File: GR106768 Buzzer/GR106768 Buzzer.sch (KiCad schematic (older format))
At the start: 65 parts, among them IC1 LMC7211, IC2 MC33172, IC3 MC33172, IC4 LMV321, J1 Conn_01x07, T1 BC847, T2 BC857, T3 BC847, T4 BC857

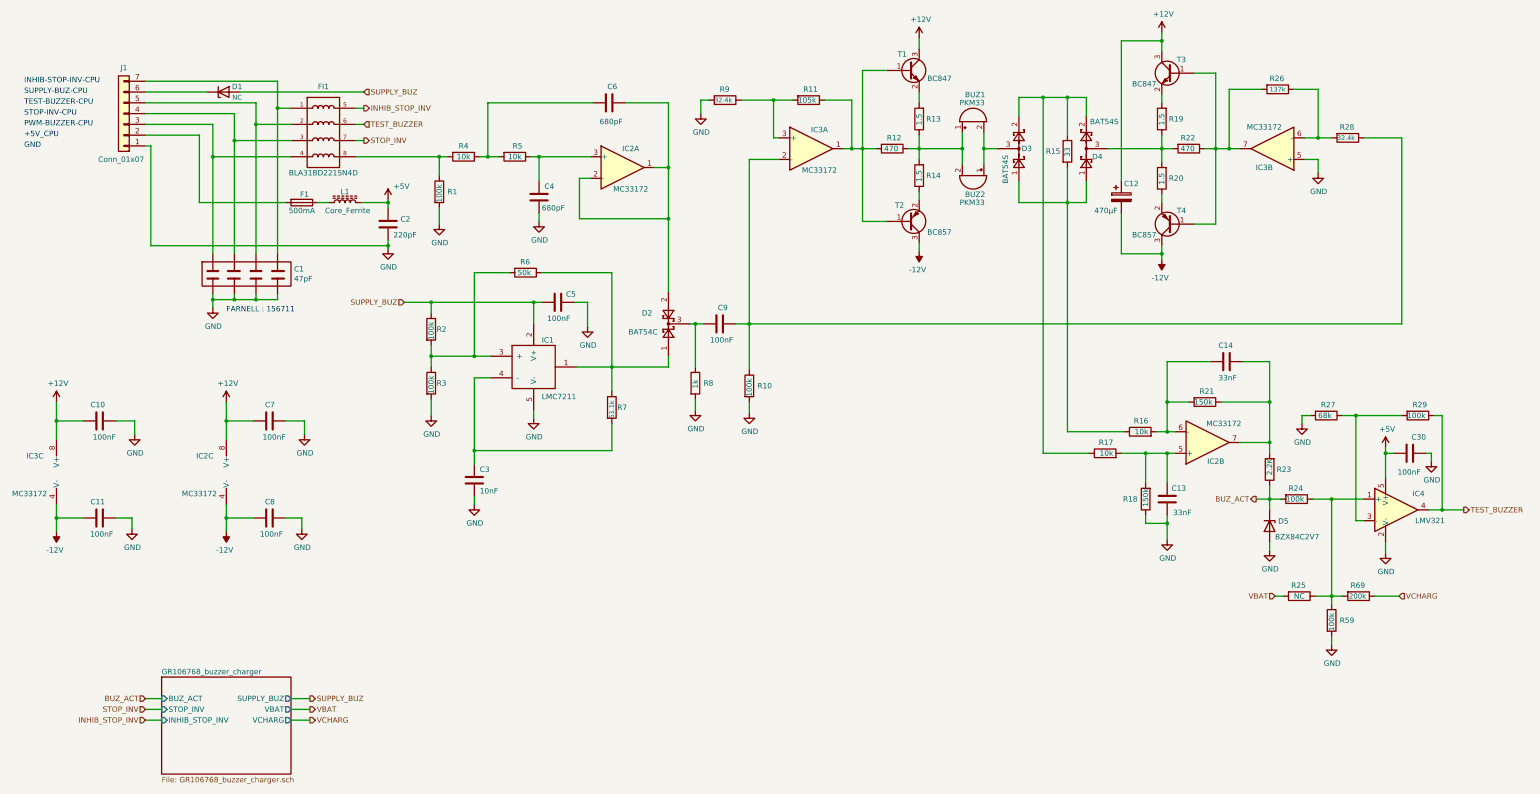
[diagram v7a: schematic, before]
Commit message: Update Buzzer schematic and cmp
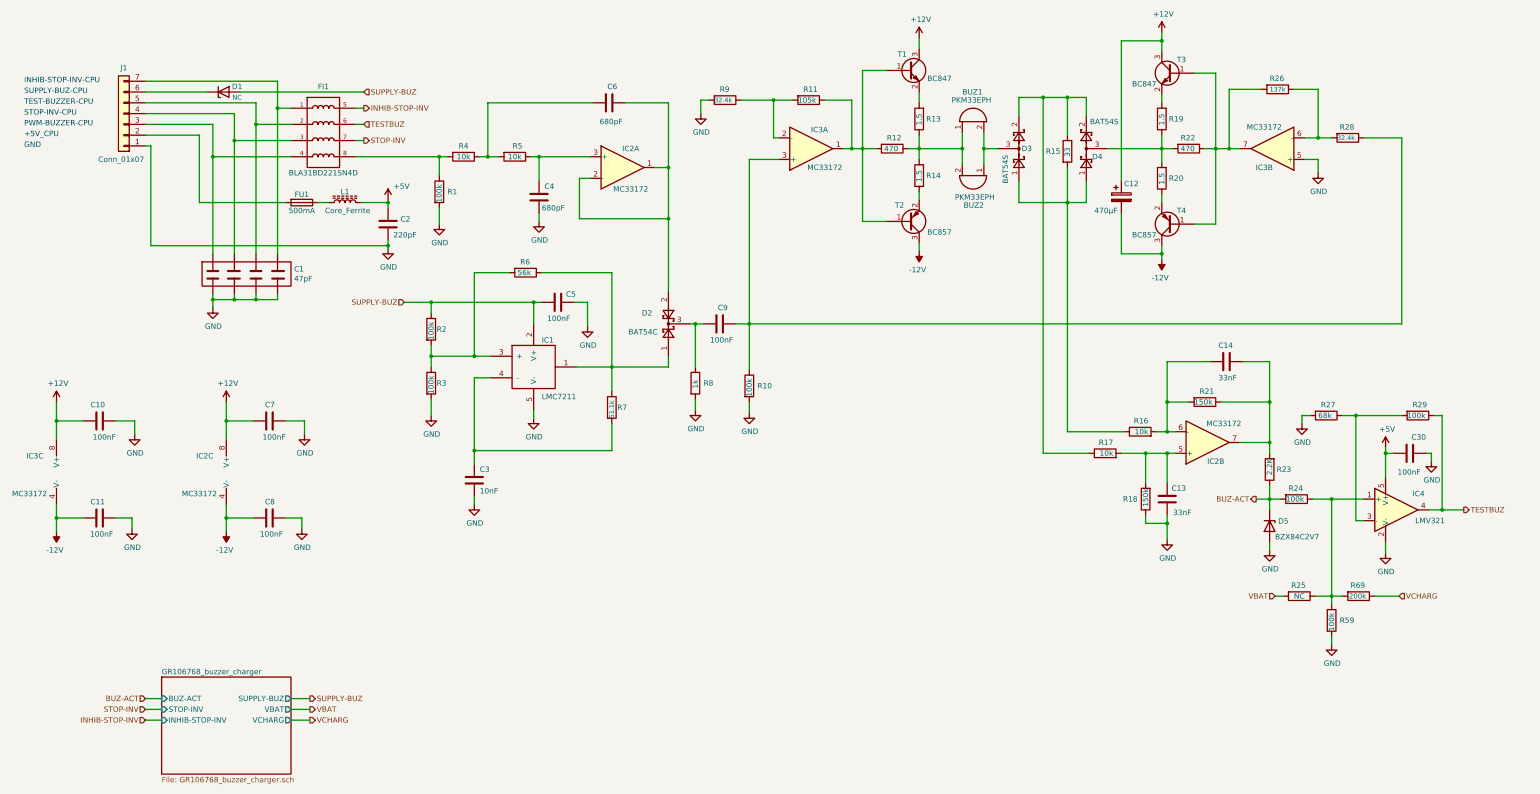
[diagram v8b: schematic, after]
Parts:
- removed BUZ1, BUZ2: PKM33, footprint_buzzer:PKM33EPH-1201C_1, symbol Device:Buzzer
- added BUZ1, BUZ2: PKM33EPH, footprint_buzzer:PKM33EPH-1201C_1, symbol buz:Buzzer
- C1: footprint footprint_buzzer:CA0612KRX7R9BB102 -> C0612-4_1
- C10, C11, C30, C4, C5, C6, C7, C9: footprint Capacitor_SMD:C_0402_1005Metric -> C0402_2
- C12: footprint Capacitor_THT:CP_Axial_L25.0mm_D10.0mm_P30.00mm_Horizontal -> AX10X30_1
- C13: footprint Capacitor_SMD:C_0402_1005Metric -> C0603_1
- C14: footprint Capacitor_SMD:C_0402_1005Metric -> C0603_2
- C2, C8: footprint Capacitor_SMD:C_0402_1005Metric -> C0402_1
- C3: footprint Capacitor_SMD:C_0402_1005Metric -> C0805_1
- D1: footprint footprint_buzzer:DIO_MBRM110LT1G -> DO216AA_1
- D2, D3, D4: footprint Package_TO_SOT_SMD:SOT-23 -> SOT23-1G_1
- D5: footprint Diode_SMD:D_SOT-23_ANK -> SOT23-1G_1
- FI1: footprint footprint_buzzer:FB_BLA31BD221SN4D -> WE-FA_1
- FU1: renamed from F1; footprint footprint_buzzer:Fuse_Littlefuse-0451_500MRL -> F6126_1
- IC1, IC4: footprint Package_TO_SOT_SMD:SOT-23-5 -> SOT23-5_1
- IC2, IC3: footprint Package_SO:PowerIntegrations_SO-8 -> MX.A8_COMPOSANT_1
- J1: footprint TerminalBlock_4Ucon:TerminalBlock_4Ucon_1x07_P3.50mm_Horizontal -> BAR7-3-2-COVIDIEN_1
- L1: footprint Inductor_SMD:L_1206_3216Metric_Pad1.42x1.75mm_HandSolder -> RC1206_1
- R1, R10, R11, R12, R13, R14, R15, R16, R17, R18, R19, R2, R20, R21, R22, R23, R24, R25, R26, R27, R28, R29, R3, R4, R5, R59, R69, R7, R8, R9: footprint Resistor_SMD:R_0402_1005Metric -> R0402_1
- R6: value 50k -> 56k; footprint Resistor_SMD:R_0402_1005Metric -> R0402_1
- T1, T2, T3, T4: footprint Package_TO_SOT_SMD:SOT-23 -> SOT23-BEC_1
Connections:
- net at R11.2, R9.1: now also IC3.2 (-); no longer IC3.3 (+)
- net at C9.2, R10.1, R28.1: now also IC3.3 (+); no longer IC3.2 (-)
- net at R12.1, R13.1, R14.2: now also BUZ1.1, BUZ2.2 (+)
- net at D3.3: now also BUZ1.2 (+), BUZ2.1
- net BUZ_ACT renamed BUZ-ACT
- net INHIB_STOP_INV renamed INHIB-STOP-INV
- net STOP_INV renamed STOP-INV
- net SUPPLY_BUZ renamed SUPPLY-BUZ
- net TEST_BUZZER renamed TESTBUZ
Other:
- note removed: "FARNELL : 156711"
